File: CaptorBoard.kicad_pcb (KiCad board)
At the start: 2 copper layers, 65 x 45 mm, 24 parts, among them J1 Conn_01x06, J2 MKDSN 1,5/ 4-5,08, SW1 SKHHLVA010, SW2 SKHHLVA010, U1 WeMos_mini, U2 IRM-02-5, U3 MOC3040X, U4 MOC3040X, U5 DHT22

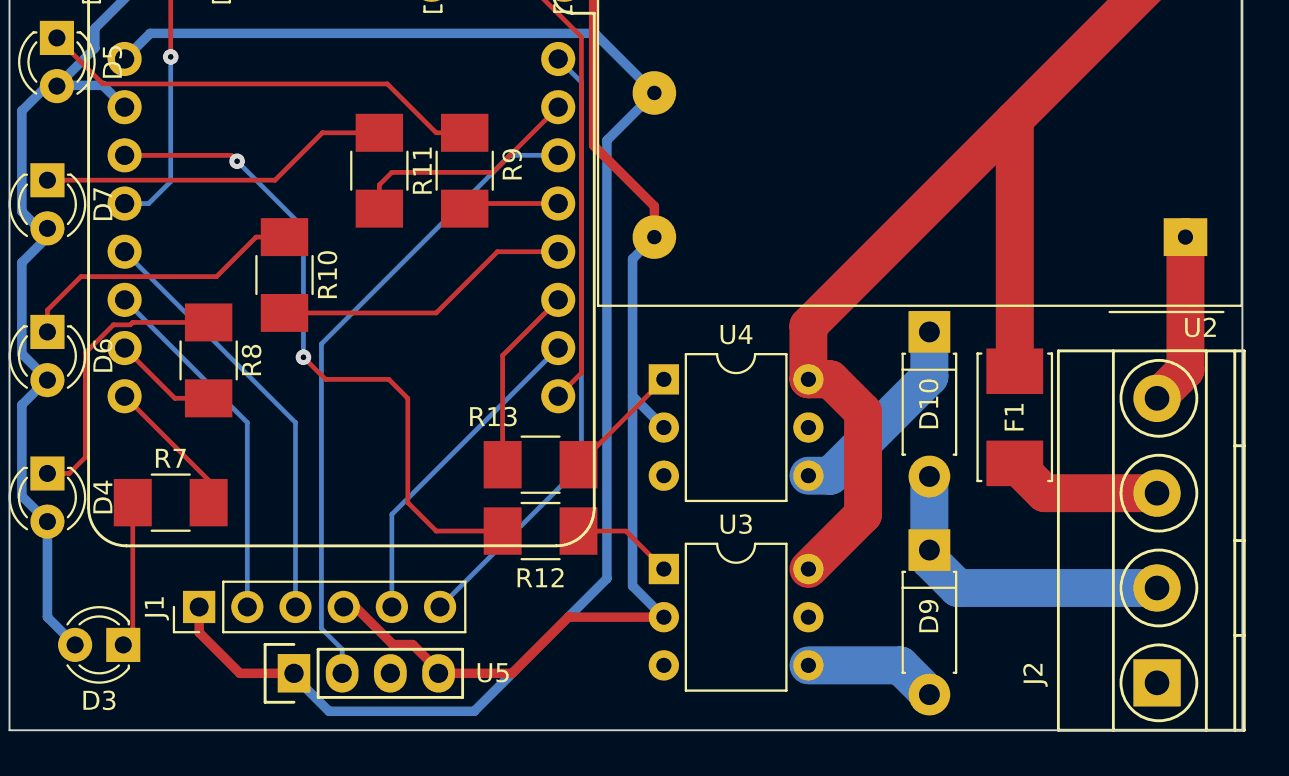
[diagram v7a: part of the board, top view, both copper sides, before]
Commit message: add pull up for booting conditions
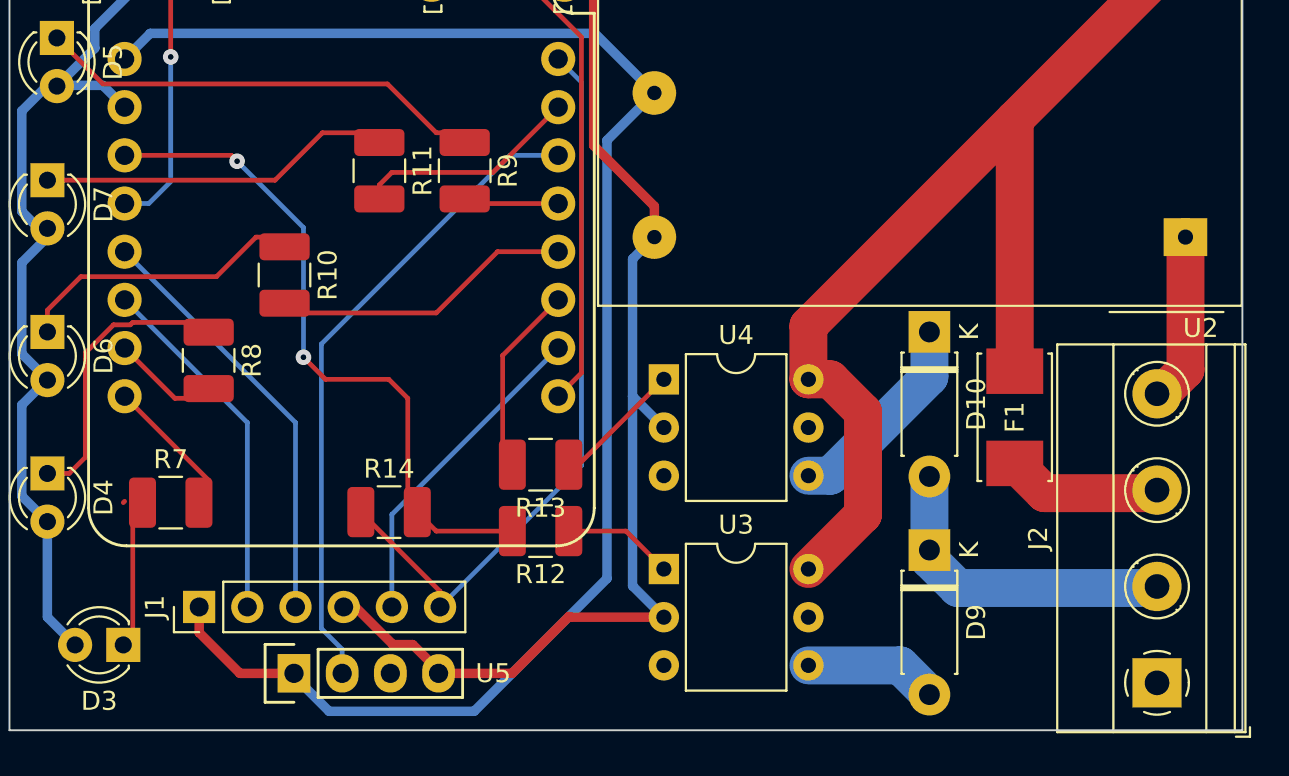
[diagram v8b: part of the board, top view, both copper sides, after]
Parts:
- added R14: 1k, Resistor_SMD:R_1210_3225Metric_Pad1.42x2.65mm_HandSolder, F.Cu at (95.0, 88.5)
- D10, D9: footprint Diodes_THT:D_DO-41_SOD81_P7.62mm_Horizontal -> Diode_THT:D_DO-41_SOD81_P7.62mm_Horizontal
- D3, D4, D5, D6, D7: footprint LEDs:LED_D3.0mm -> LED_THT:LED_D3.0mm
- J1: footprint Pin_Headers:Pin_Header_Straight_1x06_Pitch2.54mm -> Connector_PinHeader_2.54mm:PinHeader_1x06_P2.54mm_Vertical
- J2: footprint TerminalBlocks_Phoenix:TerminalBlock_Phoenix_MKDS1.5-4pol -> TerminalBlock_Phoenix:TerminalBlock_Phoenix_MKDS-1,5-4-5.08_1x04_P5.08mm_Horizontal
- R10, R11, R12, R13, R7, R8, R9: footprint Resistors_SMD:R_1210_HandSoldering -> Resistor_SMD:R_1210_3225Metric_Pad1.42x2.65mm_HandSolder
- SW1, SW2: footprint Buttons_Switches_THT:SW_Tactile_SKHH_Angled -> Button_Switch_THT:SW_Tactile_SKHH_Angled
- U2: footprint Converters_DCDC_ACDC:ACDC-Conv_THTMeanWell-IRM-02-XX -> Converter_ACDC:Converter_ACDC_MeanWell_IRM-02-xx_THT
- U3, U4: footprint Housings_DIP:DIP-6_W7.62mm -> Package_DIP:DIP-6_W7.62mm
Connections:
- J2 pad 1: (no net) -> /CMD1
- U3 pad 3: (no net) -> Net-(U3-Pad3)
- U3 pad 5: (no net) -> Net-(U3-Pad5)
- U4 pad 3: (no net) -> Net-(U4-Pad3)
- U4 pad 5: (no net) -> Net-(U4-Pad5)
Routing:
- net +3V3: track 32.5 -> 39.2 mm
